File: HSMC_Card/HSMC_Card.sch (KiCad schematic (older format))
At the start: 1 part, among them J1 HSMC_Card_ASP

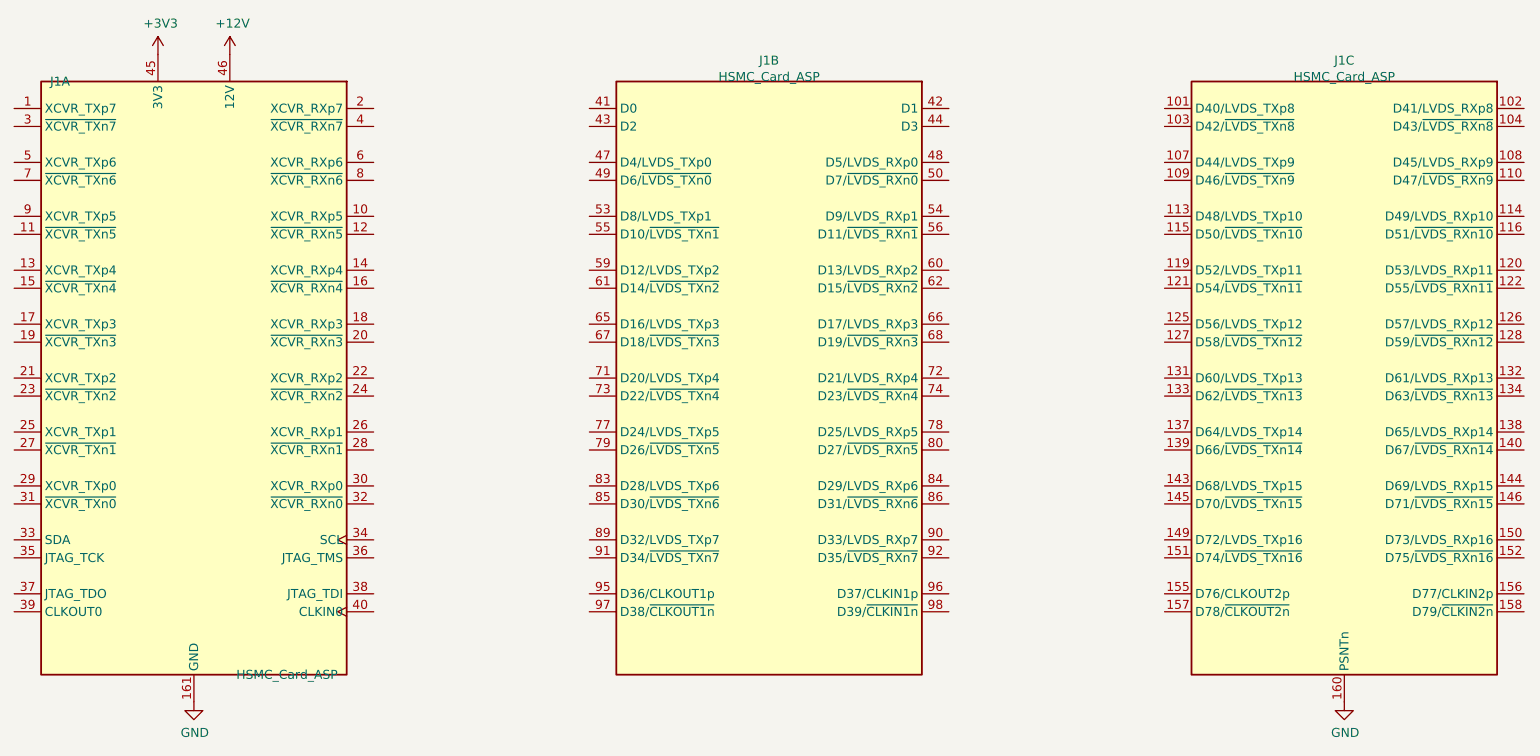
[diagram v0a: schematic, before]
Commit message: Update version of HSMC_Card_ASP symbol, minor adjustments to PCB layout template.
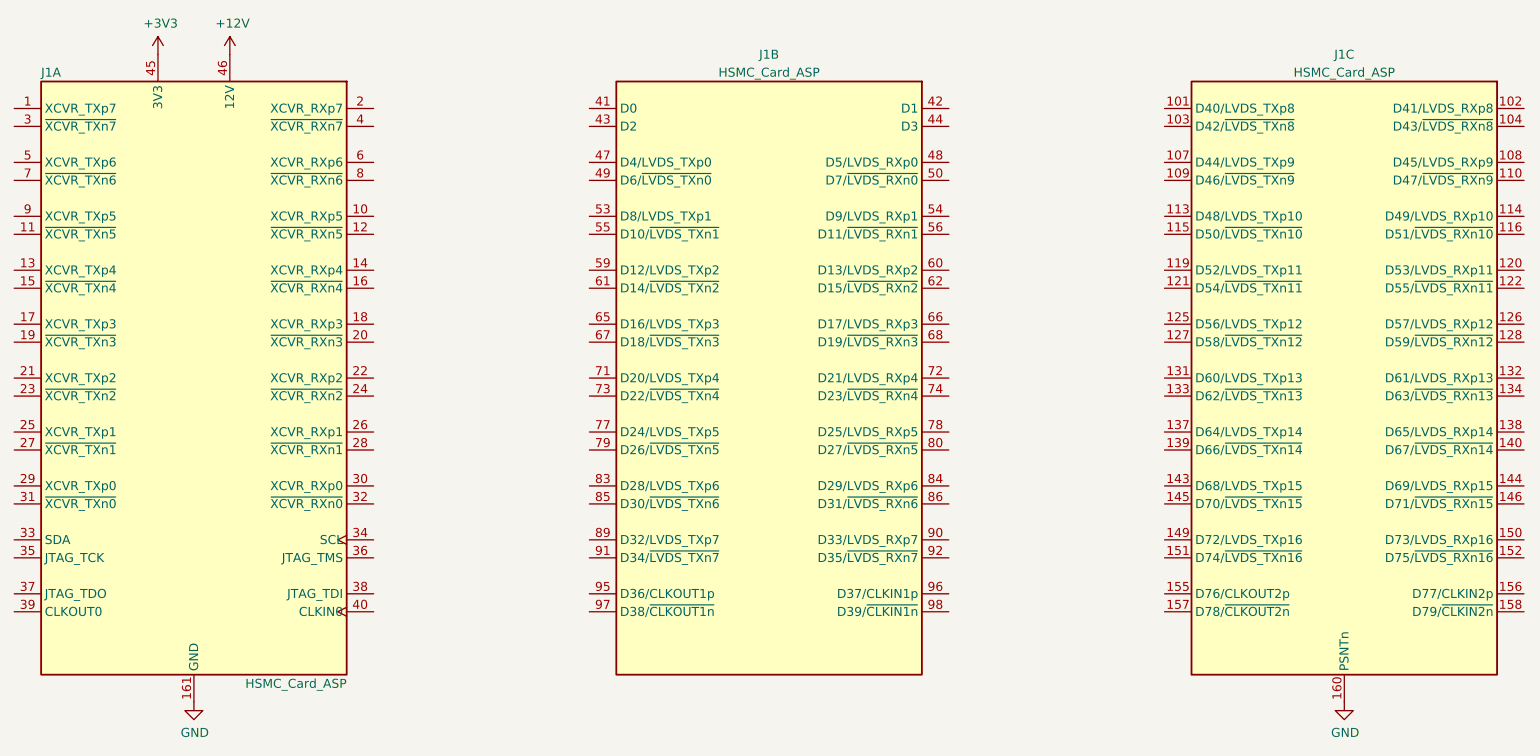
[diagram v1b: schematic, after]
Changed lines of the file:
@@
 EESchema Schematic File Version 4
 LIBS:HSMC_Card-cache
-EELAYER 26 0
+EELAYER 29 0
 EELAYER END
 $Descr A4 11693 8268
@@
 U 1 1 5C4770A2
 P 2600 2700
-F 0 "J1" H 1800 4350 50  0000 L CNN
-F 1 "HSMC_Card_ASP" H 3400 1050 50  0000 R CNN
+F 0 "J1" H 1750 4400 50  0000 L CNN
+F 1 "HSMC_Card_ASP" H 3450 1000 50  0000 R CNN
 F 2 "Connector_Samtec:Samtec_HSMC_ASP-122952-01_P0.5mm_Vertical" H 1700 4550 50  0001 C CNN
 F 3 "" H 2750 4550 50  0001 C CNN
@@
 U 2 1 5C477142
 P 5800 2700
-F 0 "J1" H 5800 4467 50  0000 C CNN
-F 1 "HSMC_Card_ASP" H 5800 4376 50  0000 C CNN
+F 0 "J1" H 5800 4500 50  0000 C CNN
+F 1 "HSMC_Card_ASP" H 5800 4400 50  0000 C CNN
 F 2 "Connector_Samtec:Samtec_HSMC_ASP-122952-01_P0.5mm_Vertical" H 4900 4550 50  0001 C CNN
 F 3 "" H 5950 4550 50  0001 C CNN
@@
 U 3 1 5C4771DF
 P 9000 2700
-F 0 "J1" H 9000 4467 50  0000 C CNN
-F 1 "HSMC_Card_ASP" H 9000 4376 50  0000 C CNN
+F 0 "J1" H 9000 4500 50  0000 C CNN
+F 1 "HSMC_Card_ASP" H 9000 4400 50  0000 C CNN
 F 2 "Connector_Samtec:Samtec_HSMC_ASP-122952-01_P0.5mm_Vertical" H 8100 4550 50  0001 C CNN
 F 3 "" H 9150 4550 50  0001 C CNN
